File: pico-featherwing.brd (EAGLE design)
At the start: 54.7 x 53.8 mm, 3 parts, among them U1 RASPBERRY_PICOSMD-TH

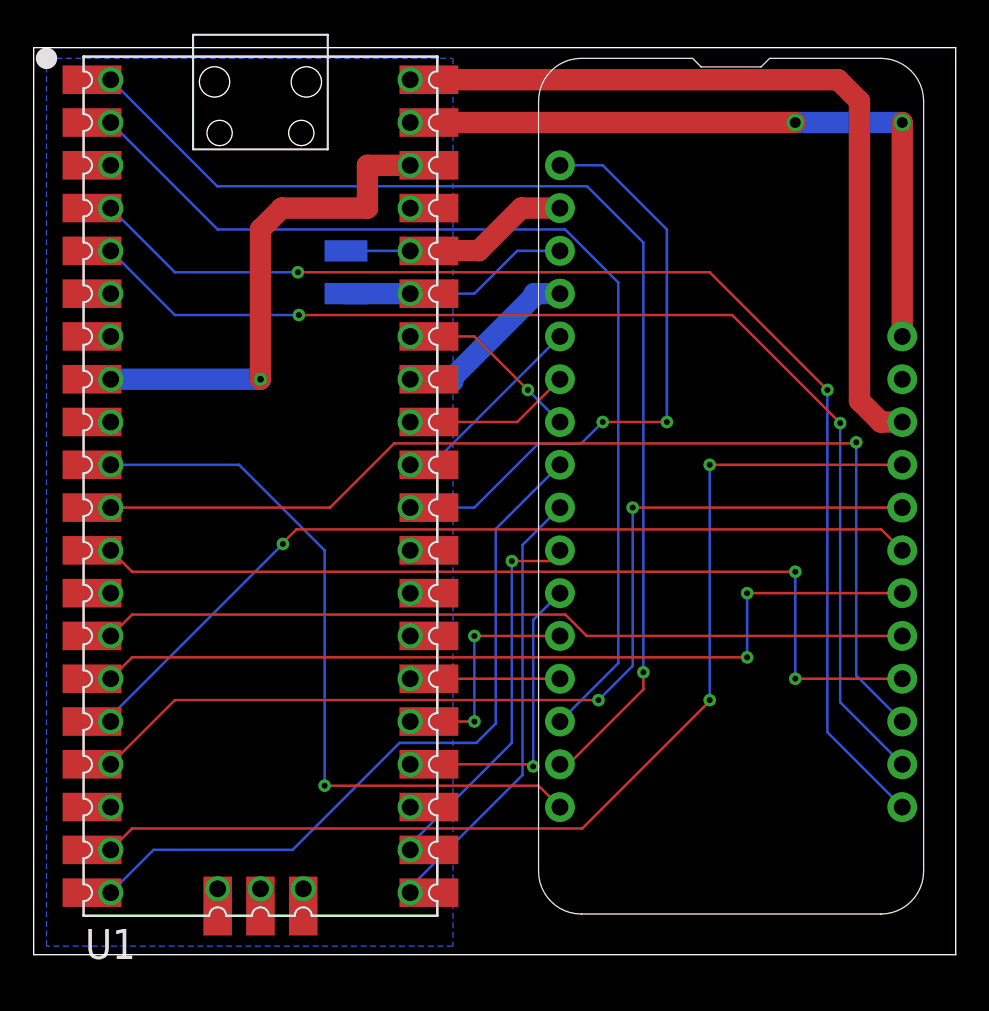
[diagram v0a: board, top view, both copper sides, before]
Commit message: Fixed pinouts, etc.
Improved ground plane and connections.
Removed ADC ref pads.
Improved 3V3 connections on FeatherWing side.
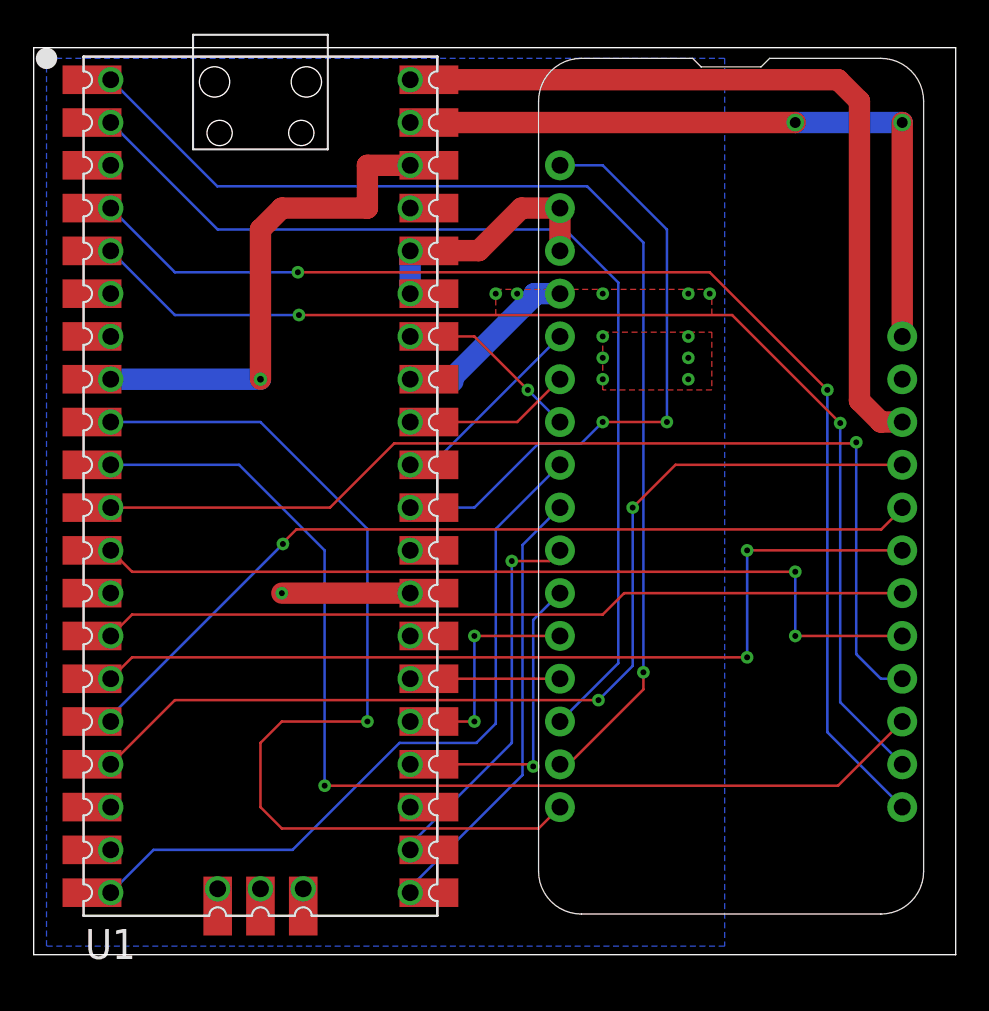
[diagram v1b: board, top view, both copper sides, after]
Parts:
- removed SJ1: AREF, jumper:SJW
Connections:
- removed net N$20: MS1.3, SJ1.2, U1.35, U1.P$35
- net +3V3: now also MS1.3, U1.35, U1.P$35; no longer SJ1.1
- net D4: now also MS1.19; no longer MS1.16
- net N$3: now also MS1.20; no longer MS1.19
- net N$4: now also MS1.21; no longer MS1.20
- net N$5: now also MS1.22; no longer MS1.21
- net N$6: now also MS1.23; no longer MS1.22
- net N$7: now also MS1.24; no longer MS1.23
- net N$8: now also MS1.25; no longer MS1.24
- net N$9: now also MS1.16, U1.9, U1.P$9; no longer MS1.25, U1.19, U1.P$19
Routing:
- net D4: track 44.4 -> 65.8 mm
- net N$20: track 14.9 -> 0.00 mm
- net GND: track 51.2 -> 59.9 mm, vias 1 -> 13
- net N$9: track 65.8 -> 59.9 mm, vias 2 -> 1
- net N$6: track 52.4 -> 55.0 mm
- net N$4: track 55.0 -> 52.4 mm
- net +3V3: track 13.8 -> 16.1 mm
- net N$3: track 64.7 -> 62.9 mm
- net N$8: track 59.9 -> 61.0 mm
- added copper zone on layer 1, net GND
